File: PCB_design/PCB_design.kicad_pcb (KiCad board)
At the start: 2 copper layers, 38 parts, among them J1 USB_B_Micro, Q1 FS8205A, U1 L298N, U2 L7805, U3 TP4056, U4 DW01A

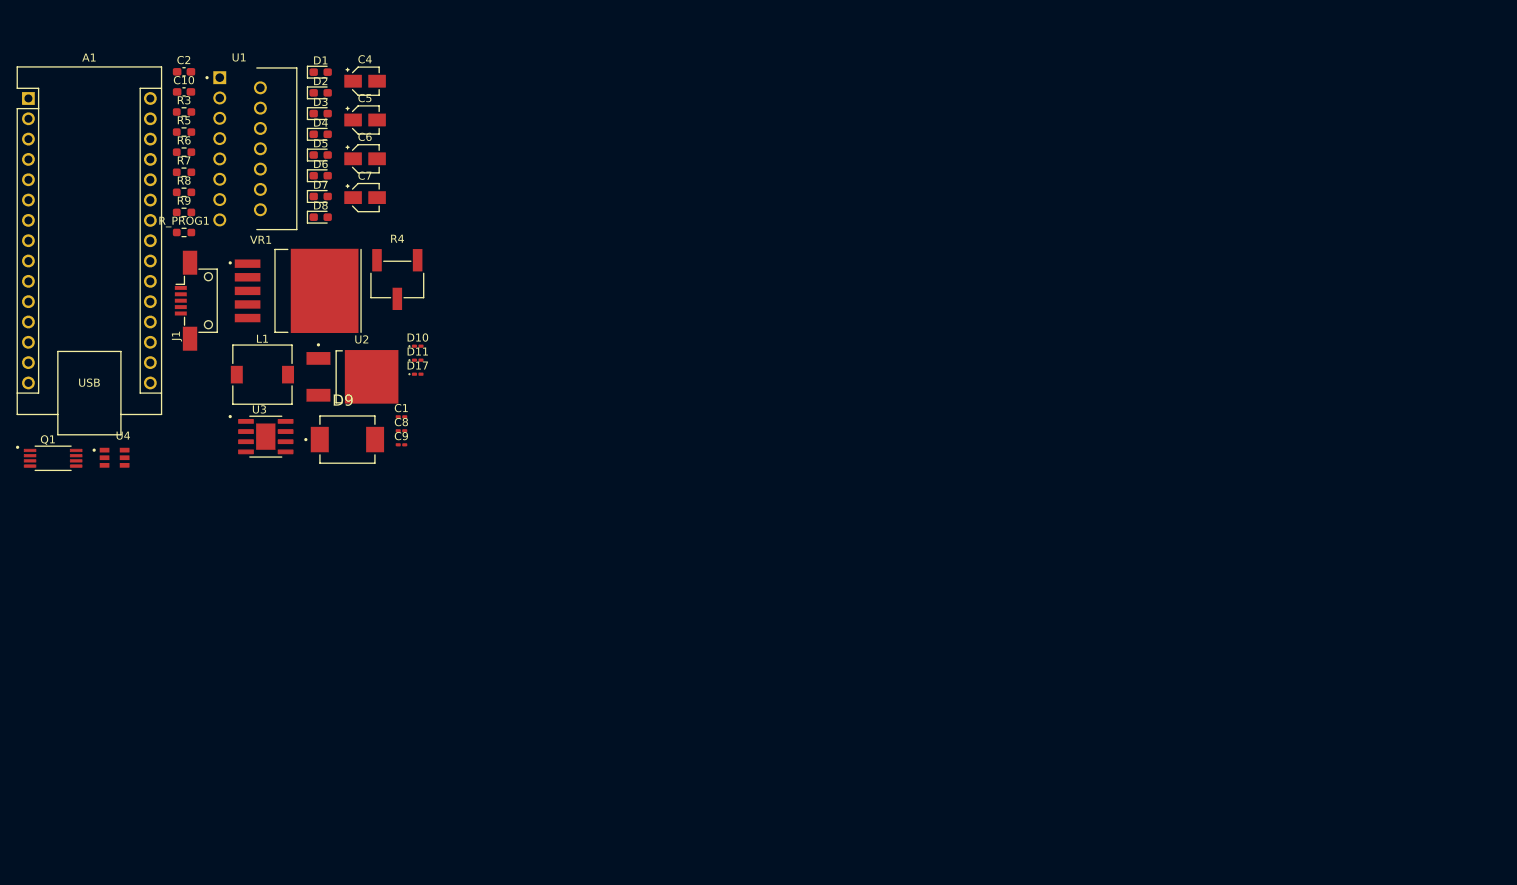
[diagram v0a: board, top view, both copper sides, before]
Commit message: Progress on PCB, added different capacitors, continued routing
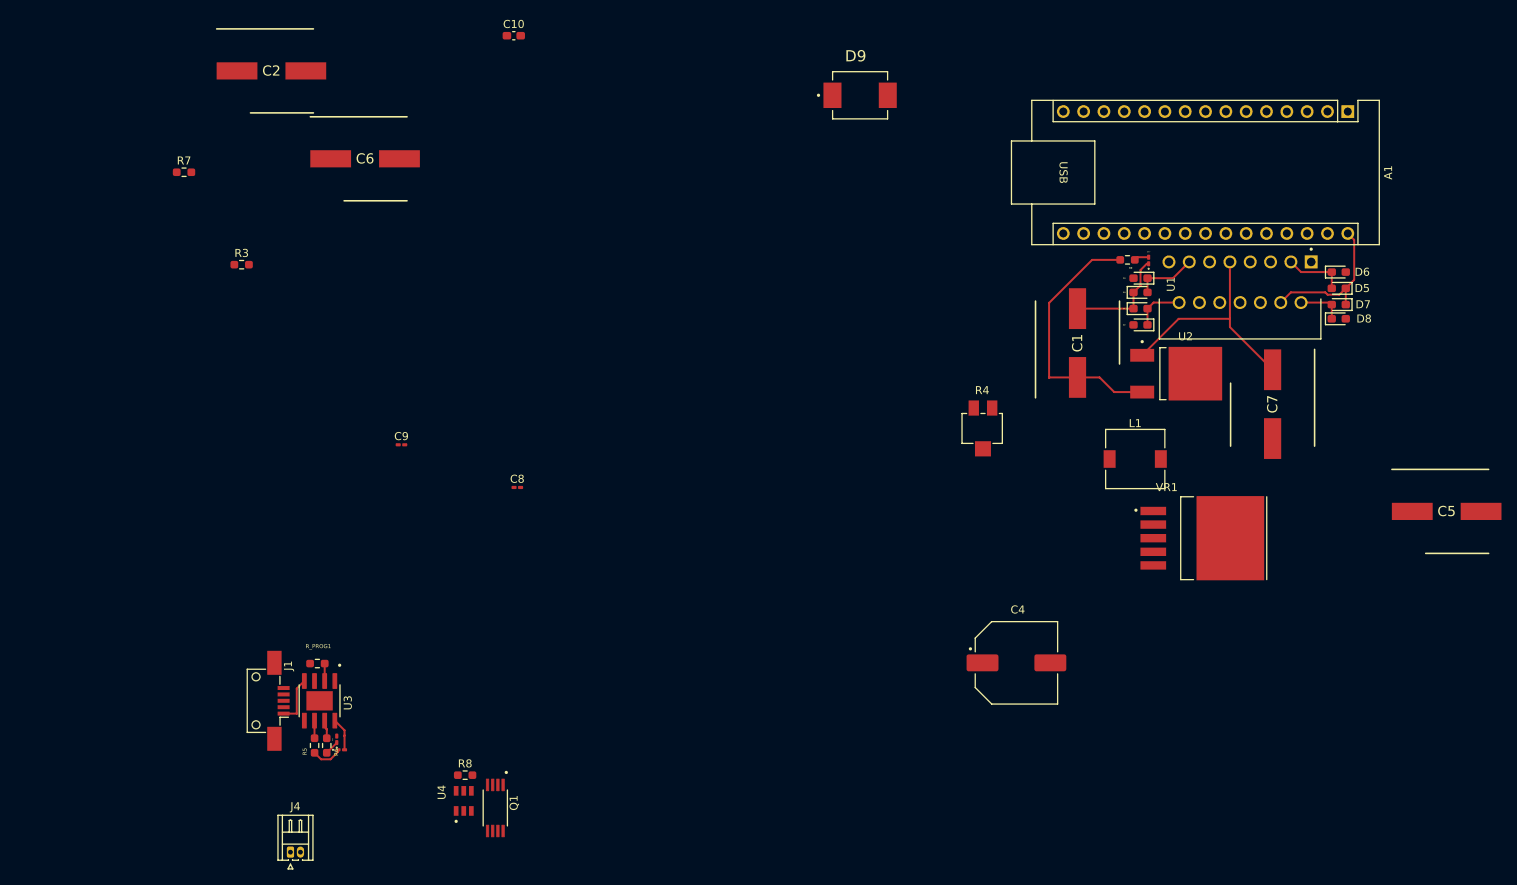
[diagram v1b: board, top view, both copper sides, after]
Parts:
- added J4: Conn_01x02_Pin, Connector_Hirose:Hirose_DF13-02P-1.25DS_1x02_P1.25mm_Horizontal, F.Cu at (60.9, 120.5)
- C1: footprint Capacitor_SMD:C_0201_0603Metric_Pad0.64x0.40mm_HandSolder -> MAL215097001E3-KiCad:CAPAE1050X1050N
- C2: footprint Capacitor_SMD:C_0603_1608Metric_Pad1.08x0.95mm_HandSolder -> MAL215097001E3-KiCad:CAPAE1050X1050N
- C4: footprint Capacitor_SMD:CP_Elec_3x5.3 -> UUD1H221MNL1GS:CAPAE1030X1080N
- C5, C6, C7: footprint Capacitor_SMD:CP_Elec_3x5.3 -> MAL215097001E3-KiCad:CAPAE1050X1050N
- R4: value R_Variable_US -> 10-25k; footprint Potentiometer_SMD:Potentiometer_Bourns_3269W_Vertical -> Potentiometer_SMD:Potentiometer_Bourns_3224X_Vertical
- moved A1 164.9 mm to (193.0, 27.9), turned to -90 degrees
- moved C5 143.8 mm to (205.4, 77.9)
- moved U1 138.4 mm to (188.5, 46.7), turned to -90 degrees
- moved D5 128.3 mm to (191.9, 50.0), turned to 180 degrees
- moved D7 128.0 mm to (191.9, 52.1), turned to 180 degrees
- moved D8 127.9 mm to (191.9, 53.8)
- moved D6 127.8 mm to (191.9, 48.0)
- moved R9 118.1 mm to (165.5, 46.5)
- moved VR1 117.4 mm to (174.9, 81.3)
- moved C7 116.3 mm to (183.6, 64.5), turned to -90 degrees
- moved L1 109.6 mm to (166.5, 71.4)
- moved C4 109.2 mm to (151.6, 96.9)
- moved D1 106.7 mm to (167.1, 52.6)
- moved D2 106.5 mm to (167.1, 54.6), turned to 180 degrees
- moved D3 104.9 mm to (167.1, 50.5)
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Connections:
- D2 pad 1: +5V -> OUT4
- D2 pad 2: OUT3 -> GND_Out
- D3 pad 2: OUT2 -> OUT3
- D4 pad 1: +5V -> OUT3
- D4 pad 2: OUT1 -> GND_Out
- D5 pad 1: OUT1 -> +5V
- D5 pad 2: GND_Out -> OUT2
- D7 pad 1: OUT3 -> +5V
- D7 pad 2: GND_Out -> OUT1
- D8 pad 1: OUT4 -> OUT1
- U1 pad 5: Net-(A1-A0) -> Net-(A1-A1)
- U1 pad 7: Net-(A1-A1) -> Net-(A1-A0)
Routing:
- net Net-(U2-OUT): track 0.00 -> 32.9 mm
- net +5V: track 0.00 -> 32.3 mm
- net Boost_Out: track 0.00 -> 28.5 mm
- net OUT3: track 0.00 -> 7.84 mm
- net OUT2: track 0.00 -> 7.67 mm
- net OUT4: track 0.00 -> 6.30 mm
- net Net-(J1-VBUS): track 0.00 -> 6.11 mm
- net OUT1: track 0.00 -> 5.72 mm
- net Net-(D10-A): track 0.00 -> 4.22 mm
- net Net-(D10-K): track 0.00 -> 3.91 mm
- net Charge: track 0.00 -> 2.34 mm
- net Hold: track 0.00 -> 2.20 mm
- net Net-(U3-PROG): track 0.00 -> 2.18 mm
- net Net-(D17-A): track 0.00 -> 1.87 mm
- net Net-(D11-K): track 0.00 -> 1.80 mm

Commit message: Finished routing of PCB, v0
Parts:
- C1, C2, C7: footprint MAL215097001E3-KiCad:CAPAE1050X1050N -> Capacitor_220uF35V_smaller:CAPAE1050X1050N
- C4: footprint UUD1H221MNL1GS:CAPAE1030X1080N -> Capacitor_220uF35V_smaller:CAPAE1050X1050N
- C5: footprint MAL215097001E3-KiCad:CAPAE1050X1050N -> Capacitor_SMD:C_0201_0603Metric_Pad0.64x0.40mm_HandSolder
- C6: footprint MAL215097001E3-KiCad:CAPAE1050X1050N -> Capacitor_SMD:C_0603_1608Metric_Pad1.08x0.95mm_HandSolder
- D9: value 1N5824 -> SS34; footprint SS34:DIOM7959X265N -> KiCad:DIOM8059X256N
- moved R7 129.3 mm to (164.9, 90.0), turned to 180 degrees
- moved J4 120.5 mm to (177.8, 91.2), turned to 90 degrees
- moved R3 118.1 mm to (169.1, 77.0)
- moved C2 111.4 mm to (140.7, 98.0), turned to 180 degrees
- moved R5 110.8 mm to (174.4, 99.4), turned to 180 degrees
- moved J1 110.5 mm to (168.8, 104.9), turned to -90 degrees
- moved C10 109.5 mm to (171.8, 90.0), turned to 90 degrees
- moved R6 109.4 mm to (174.4, 97.9), turned to 180 degrees
- moved D10 108.3 mm to (174.9, 96.1), turned to 90 degrees
- moved C6 108.2 mm to (172.6, 68.9)
- moved D11 107.4 mm to (173.6, 96.7), turned to 180 degrees
- moved U3 104.3 mm to (168.8, 98.8), turned to 0 degrees
- moved C9 102.4 mm to (174.3, 93.8), turned to 180 degrees
- moved R_PROG1 100.0 mm to (164.2, 99.1), turned to -90 degrees
- moved U4 89.6 mm to (168.8, 90.1), turned to 0 degrees
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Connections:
- A1 pad 29: GND_Out -> Batt-
- A1 pad 4: GND_Out -> Batt-
- C2 pad 2: GND_Out -> Batt-
- C4 pad 2: GND_Out -> Batt-
- C5 pad 2: GND_Out -> Batt-
- C6 pad 2: GND_Out -> Batt-
- C7 pad 2: GND_Out -> Batt-
- C8 pad 2: GND_Out -> Batt-
- C9 pad 2: GND_Out -> Batt-
- D2 pad 2: GND_Out -> Batt-
- D4 pad 2: GND_Out -> Batt-
- D6 pad 2: GND_Out -> Batt-
- D8 pad 2: GND_Out -> Batt-
- J1 pad 5: GND_Out -> Batt-
- Q1 pad 6: GND_Out -> Batt-
- Q1 pad 7: GND_Out -> Batt-
- R3 pad 2: GND_Out -> Batt-
- R7 pad 2: GND_Out -> Batt-
- R_PROG1 pad 2: GND_Out -> Batt-
- U1 pad 1: GND_Out -> Batt-
- U1 pad 11: GND_Out -> Batt-
- U1 pad 15: GND_Out -> Batt-
- U1 pad 5: Net-(A1-A1) -> Net-(A1-A0)
- U1 pad 6: GND_Out -> Batt-
- U1 pad 7: Net-(A1-A0) -> Net-(A1-A1)
- U1 pad 8: GND_Out -> Batt-
- U2 pad 2: GND_Out -> Batt-
- U3 pad 1: GND_Out -> Batt-
- U3 pad 3: GND_Out -> Batt-
- VR1 pad 1: GND_Out -> Batt-
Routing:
- net Batt-: track 0.00 -> 235.9 mm
- net Bat+: track 0.00 -> 53.0 mm
- net +5V: track 32.3 -> 62.5 mm
- net Net-(D9-B): track 0.00 -> 30.2 mm
- net Boost_Out: track 28.5 -> 47.2 mm
- net Net-(A1-A1): track 0.00 -> 15.8 mm
- net Net-(A1-A0): track 0.00 -> 12.2 mm
- net Net-(U4-OD): track 0.00 -> 7.53 mm
- net Net-(U4-VCC): track 0.00 -> 6.06 mm
- net Net-(Q1-Pad1): track 0.00 -> 5.76 mm
- net OUT2: track 7.67 -> 2.07 mm
- net OUT1: track 5.72 -> 10.8 mm
- net Net-(VR1-FB): track 0.00 -> 4.16 mm
- net Net-(U4-OC): track 0.00 -> 2.79 mm
- net Net-(U4-CS): track 0.00 -> 1.78 mm
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
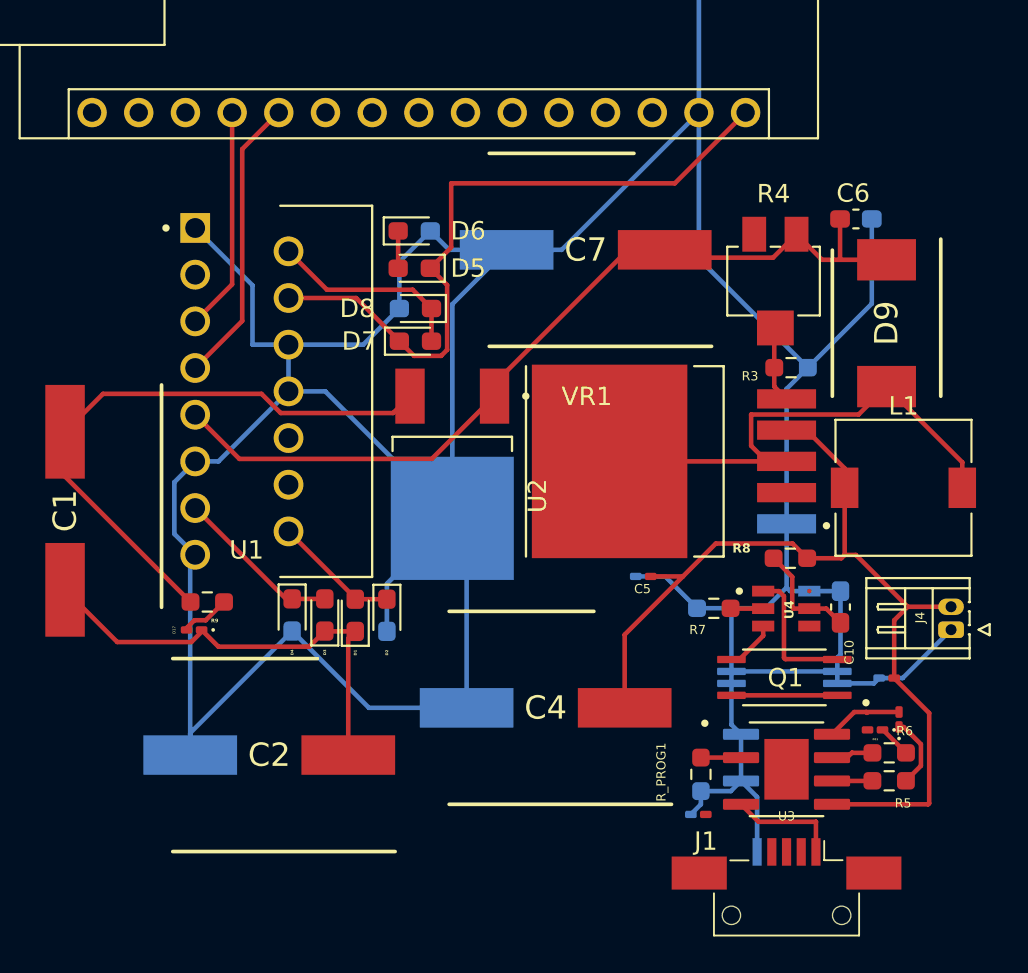
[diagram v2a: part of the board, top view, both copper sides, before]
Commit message: Fixed routing to bottom layer
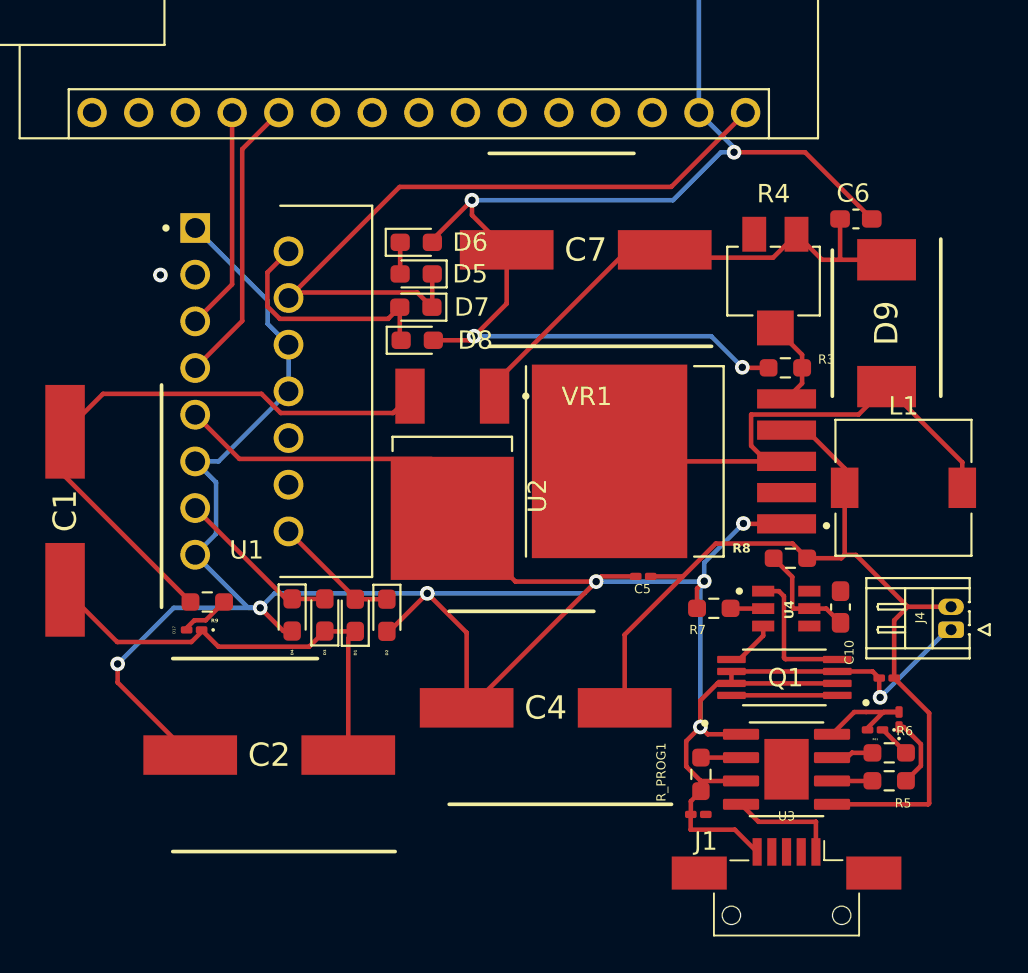
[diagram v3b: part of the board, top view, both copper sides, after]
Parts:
- moved D7 1.85 mm to (148.7, 73.7), turned to 180 degrees
- moved D8 1.73 mm to (148.7, 75.5), turned to 0 degrees
- moved D6 0.63 mm to (148.7, 70.1)
- moved D5 0.33 mm to (148.7, 71.8)
- moved R3 0.31 mm to (168.8, 77.0), turned to 180 degrees
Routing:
- net Boost_Out: track 47.2 -> 42.4 mm
- net OUT1: track 10.8 -> 13.0 mm
- net Net-(D10-A): track 4.22 -> 6.33 mm
- net +5V: track 62.5 -> 64.1 mm
- net Batt-: track 235.9 -> 234.9 mm, vias 0 -> 12
- net Net-(VR1-FB): track 4.16 -> 4.90 mm
- net (no net): vias 0 -> 1

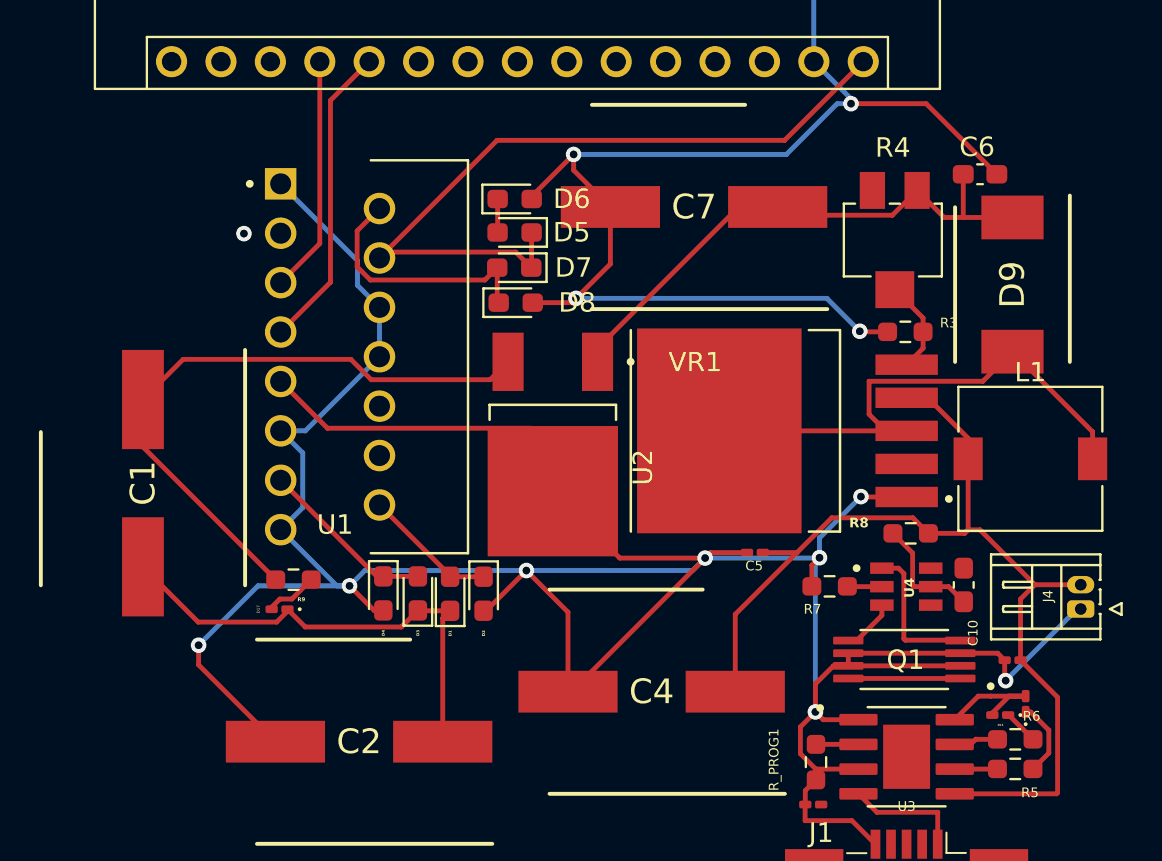
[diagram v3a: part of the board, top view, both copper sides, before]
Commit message: Removed GND to Bat- connection and rereouted
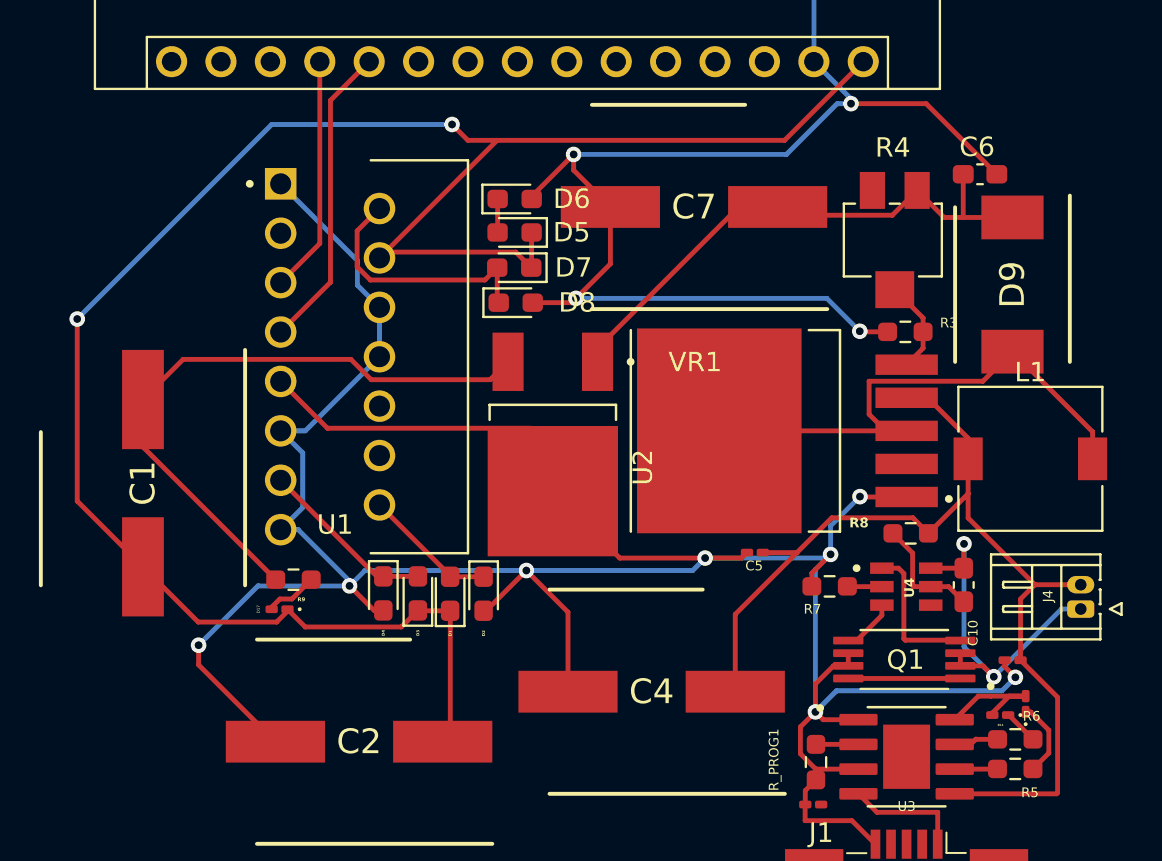
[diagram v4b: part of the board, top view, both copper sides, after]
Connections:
- A1 pad 29: Batt- -> GND_Out
- A1 pad 4: Batt- -> GND_Out
- C2 pad 2: Batt- -> GND_Out
- C4 pad 2: Batt- -> GND_Out
- C5 pad 2: Batt- -> GND_Out
- C6 pad 2: Batt- -> GND_Out
- C7 pad 2: Batt- -> GND_Out
- C8 pad 2: Batt- -> GND_Out
- C9 pad 2: Batt- -> GND_Out
- D2 pad 2: Batt- -> GND_Out
- D4 pad 2: Batt- -> GND_Out
- D6 pad 2: Batt- -> GND_Out
- D8 pad 2: Batt- -> GND_Out
- J1 pad 5: Batt- -> GND_Out
- Q1 pad 6: Batt- -> GND_Out
- Q1 pad 7: Batt- -> GND_Out
- R3 pad 2: Batt- -> GND_Out
- R7 pad 2: Batt- -> GND_Out
- R_PROG1 pad 2: Batt- -> GND_Out
- U1 pad 1: Batt- -> GND_Out
- U1 pad 11: Batt- -> GND_Out
- U1 pad 15: Batt- -> GND_Out
- U1 pad 6: Batt- -> GND_Out
- U1 pad 8: Batt- -> GND_Out
- U1 pad 9: Boost_Out -> GND_Out
- U2 pad 2: Batt- -> GND_Out
- U3 pad 1: Batt- -> GND_Out
- U3 pad 3: Batt- -> GND_Out
- VR1 pad 1: Batt- -> GND_Out
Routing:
- net GND_Out: track 0.00 -> 232.0 mm, vias 0 -> 12
- net Batt-: track 234.9 -> 18.9 mm, vias 12 -> 2
- net +5V: track 64.1 -> 104.3 mm, vias 0 -> 2
- net Boost_Out: track 42.4 -> 28.5 mm
- net (no net): vias 1 -> 0
